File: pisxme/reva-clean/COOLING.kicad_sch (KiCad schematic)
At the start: 0 parts

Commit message: add native Phase 3 contract connectivity
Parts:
- added X: COOLING_Contract
- added XCO: COOLING_Contract, symbol PiSXMeRevAClean:COOLING_Contract
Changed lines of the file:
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@@
 (kicad_sch (version 20230409) (generator "eeschema")
   (paper "A4")
+    (symbol "PiSXMeRevAClean:COOLING_Contract"
+      (pin_names (offset 1.0))
+      (exclude_from_sim no)
+      (in_bom yes)
+      (on_board yes)
+      (property "Reference" "X"
+        (at 0 -7.039999999999999 0)
+        (effects (font (size 1.27 1.27))))
+      (property "Value" "COOLING_Contract"
+        (at 0 7.039999999999999 0)
+        (effects (font (size 1.27 1.27))))
+      (property "Footprint" ""
+        (at 0 0 0)
+        (effects (font (size 1.27 1.27)) (hide yes)))
+      (property "Datasheet" "~"
+        (at 0 0 0)
+        (effects (font (size 1.27 1.27)) (hide yes)))
+      (symbol "COOLING_Contract_1_1"
+        (rectangle (start -1.27 -5.77) (end 1.27 5.77)
+          (stroke (width 0.254) (type default)) (fill (type background)))
+        (pin passive line
+          (at -5.08 0 0)
+          (length 3.81)
+          (name "COOLING_12V" (effects (font (size 1.27 1.27))))
+          (number "1" (effects (font (size 1.27 1.27)))))
+        (pin passive line
+          (at -5.08 3 0)
+          (length 3.81)
+          (name "COOLING_PWM" (effects (font (size 1.27 1.27))))
+          (number "2" (effects (font (size 1.27 1.27)))))
+        (pin passive line
+          (at -5.08 6 0)
+          (length 3.81)
+          (name "COOLING_TACH" (effects (font (size 1.27 1.27))))
+          (number "3" (effects (font (size 1.27 1.27)))))
+        (pin passive line
+          (at -5.08 9 0)
+          (length 3.81)
+          (name "THERMAL_ALERT" (effects (font (size 1.27 1.27))))
+          (number "4" (effects (font (size 1.27 1.27)))))
+      )
+    )
   (hierarchical_label "COOLING_12V"
     (shape bidirectional)
@@
     (effects (font (size 1.27 1.27)) (justify left))
 )
-  (sheet_instances (path "/9" (page "9")))
+  (wire
+    (pts (xy 5 10) (xy 19.92 10))
+    (stroke (width 0) (type default))
 )
+  (wire
+    (pts (xy 5 13) (xy 19.92 13))
+    (stroke (width 0) (type default))
+)
+  (wire
+    (pts (xy 5 16) (xy 19.92 16))
+    (stroke (width 0) (type default))
+)
+  (wire
+    (pts (xy 5 19) (xy 19.92 19))
+    (stroke (width 0) (type default))
+)
+  (symbol
+    (lib_id "PiSXMeRevAClean:COOLING_Contract")
+    (at 25 10 0)
+    (unit 1)
+    (exclude_from_sim no)
+    (in_bom no)
+    (on_board no)
+    (dnp no)
+    (property "Reference" "XCO"
+      (at 25 5 0)
+      (effects (font (size 1.27 1.27))))
+    (property "Value" "COOLING_Contract"
+      (at 25 18 0)
+      (effects (font (size 1.27 1.27))))
+    (property "Footprint" ""
+      (at 25 10 0)
+      (effects (font (size 1.27 1.27)) (hide yes)))
+    (property "Datasheet" "~"
+      (at 25 10 0)
+      (effects (font (size 1.27 1.27)) (hide yes)))
+    (pin "1")
+    (pin "2")
+    (pin "3")
+    (pin "4")
+    (instances (project "PiSXMe_RevA_Clean"
+      (path "/30000000-0000-0000-0000-000000000000/10000000-0000-0000-0000-000000000009" (reference "XCO" ) (unit 1))))
+  )
+  (sheet_instances (path "/30000000-0000-0000-0000-000000000000/10000000-0000-0000-0000-000000000009" (page "9")))
+)

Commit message: close native Phase 3 hierarchy association
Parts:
- removed X: COOLING_Contract
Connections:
- net COOLING_12V: now also XCO.1 (COOLING_12V)
- net COOLING_PWM: now also XCO.2 (COOLING_PWM)
- net COOLING_TACH: now also XCO.3 (COOLING_TACH)
- net THERMAL_ALERT: now also XCO.4 (THERMAL_ALERT)
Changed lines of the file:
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@@
 (kicad_sch (version 20230409) (generator "eeschema")
   (paper "A4")
-    (symbol "PiSXMeRevAClean:COOLING_Contract"
-      (pin_names (offset 1.0))
-      (exclude_from_sim no)
-      (in_bom yes)
-      (on_board yes)
-      (property "Reference" "X"
-        (at 0 -7.039999999999999 0)
-        (effects (font (size 1.27 1.27))))
-      (property "Value" "COOLING_Contract"
-        (at 0 7.039999999999999 0)
-        (effects (font (size 1.27 1.27))))
-      (property "Footprint" ""
-        (at 0 0 0)
-        (effects (font (size 1.27 1.27)) (hide yes)))
-      (property "Datasheet" "~"
-        (at 0 0 0)
-        (effects (font (size 1.27 1.27)) (hide yes)))
-      (symbol "COOLING_Contract_1_1"
-        (rectangle (start -1.27 -5.77) (end 1.27 5.77)
-          (stroke (width 0.254) (type default)) (fill (type background)))
-        (pin passive line
-          (at -5.08 0 0)
-          (length 3.81)
-          (name "COOLING_12V" (effects (font (size 1.27 1.27))))
-          (number "1" (effects (font (size 1.27 1.27)))))
-        (pin passive line
-          (at -5.08 3 0)
-          (length 3.81)
-          (name "COOLING_PWM" (effects (font (size 1.27 1.27))))
-          (number "2" (effects (font (size 1.27 1.27)))))
-        (pin passive line
-          (at -5.08 6 0)
-          (length 3.81)
-          (name "COOLING_TACH" (effects (font (size 1.27 1.27))))
-          (number "3" (effects (font (size 1.27 1.27)))))
-        (pin passive line
-          (at -5.08 9 0)
-          (length 3.81)
-          (name "THERMAL_ALERT" (effects (font (size 1.27 1.27))))
-          (number "4" (effects (font (size 1.27 1.27)))))
-      )
-    )
   (hierarchical_label "COOLING_12V"
     (shape bidirectional)
-    (at 5 10 0)
-    (effects (font (size 1.27 1.27)) (justify left))
+    (at 5 10 180)
+    (effects (font (size 1.27 1.27)) (justify right))
 )
   (hierarchical_label "COOLING_PWM"
     (shape bidirectional)
-    (at 5 13 0)
-    (effects (font (size 1.27 1.27)) (justify left))
+    (at 5 13 180)
+    (effects (font (size 1.27 1.27)) (justify right))
 )
   (hierarchical_label "COOLING_TACH"
     (shape bidirectional)
-    (at 5 16 0)
-    (effects (font (size 1.27 1.27)) (justify left))
+    (at 5 16 180)
+    (effects (font (size 1.27 1.27)) (justify right))
 )
   (hierarchical_label "THERMAL_ALERT"
     (shape bidirectional)
-    (at 5 19 0)
-    (effects (font (size 1.27 1.27)) (justify left))
+    (at 5 19 180)
+    (effects (font (size 1.27 1.27)) (justify right))
 )
   (wire

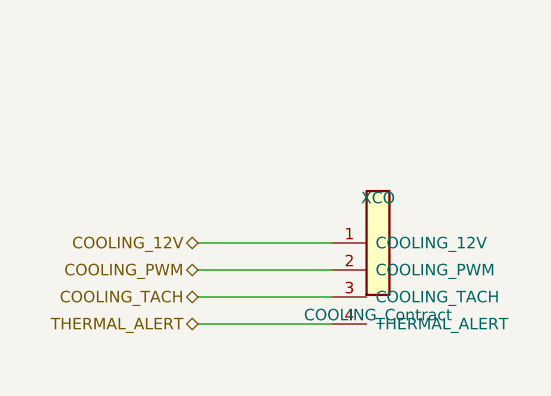
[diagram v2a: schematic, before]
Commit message: stabilize Phase 3 hierarchy netlist references
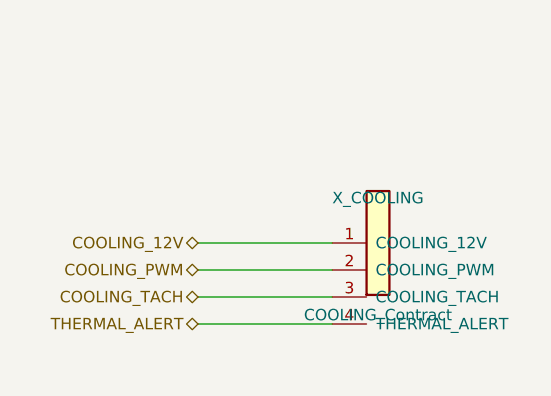
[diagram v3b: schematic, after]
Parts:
- renumbered XCO to X_COOLING
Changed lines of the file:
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@@
     (on_board no)
     (dnp no)
-    (property "Reference" "XCO"
+    (property "Reference" "X_COOLING"
       (at 25 5 0)
       (effects (font (size 1.27 1.27))))
@@
     (pin "4")
     (instances (project "PiSXMe_RevA_Clean"
-      (path "/30000000-0000-0000-0000-000000000000/10000000-0000-0000-0000-000000000009" (reference "XCO" ) (unit 1))))
+      (path "/30000000-0000-0000-0000-000000000000/10000000-0000-0000-0000-000000000009" (reference "X_COOLING" ) (unit 1))))
   )
   (sheet_instances (path "/30000000-0000-0000-0000-000000000000/10000000-0000-0000-0000-000000000009" (page "9")))

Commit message: fix KiCad annotation and netlist export
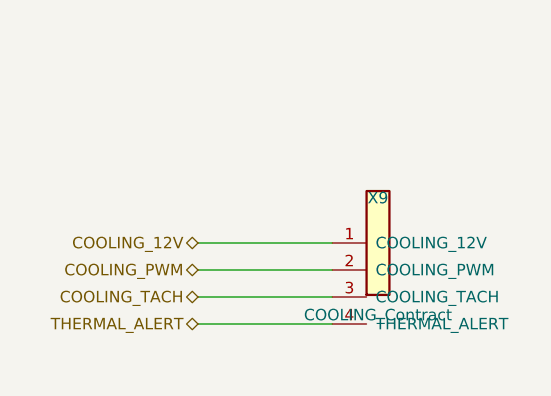
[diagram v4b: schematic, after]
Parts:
- renumbered X_COOLING to X9
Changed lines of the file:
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@@
     (on_board no)
     (dnp no)
-    (property "Reference" "X_COOLING"
+    (property "Reference" "X9"
       (at 25 5 0)
       (effects (font (size 1.27 1.27))))
@@
     (pin "4")
     (instances (project "PiSXMe_RevA_Clean"
-      (path "/30000000-0000-0000-0000-000000000000/10000000-0000-0000-0000-000000000009" (reference "X_COOLING" ) (unit 1))))
+      (path "/30000000-0000-0000-0000-000000000000/10000000-0000-0000-0000-000000000009" (reference "X9" ) (unit 1))))
   )
   (sheet_instances (path "/30000000-0000-0000-0000-000000000000/10000000-0000-0000-0000-000000000009" (page "9")))

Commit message: phase24: promote identity-preserving hierarchy repair
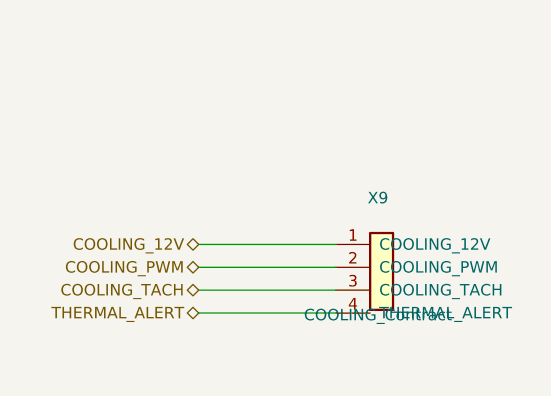
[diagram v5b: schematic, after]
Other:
- moved on the sheet: X9
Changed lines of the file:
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@@
   (hierarchical_label "COOLING_12V"
     (shape bidirectional)
-    (at 5 10 180)
+    (at 5.08 10.16 180)
     (effects (font (size 1.27 1.27)) (justify right))
 )
   (hierarchical_label "COOLING_PWM"
     (shape bidirectional)
-    (at 5 13 180)
+    (at 5.08 12.7 180)
     (effects (font (size 1.27 1.27)) (justify right))
 )
   (hierarchical_label "COOLING_TACH"
     (shape bidirectional)
-    (at 5 16 180)
+    (at 5.08 15.24 180)
     (effects (font (size 1.27 1.27)) (justify right))
 )
   (hierarchical_label "THERMAL_ALERT"
     (shape bidirectional)
-    (at 5 19 180)
+    (at 5.08 17.78 180)
     (effects (font (size 1.27 1.27)) (justify right))
 )
   (wire
-    (pts (xy 5 10) (xy 19.92 10))
+    (pts (xy 5.08 10.16) (xy 20.32 10.16))
     (stroke (width 0) (type default))
 )
   (wire
-    (pts (xy 5 13) (xy 19.92 13))
+    (pts (xy 5.08 12.7) (xy 20.32 12.7))
     (stroke (width 0) (type default))
 )
   (wire
-    (pts (xy 5 16) (xy 19.92 16))
+    (pts (xy 5.08 15.24) (xy 20.32 15.24))
     (stroke (width 0) (type default))
 )
   (wire
-    (pts (xy 5 19) (xy 19.92 19))
+    (pts (xy 5.08 17.78) (xy 20.32 17.78))
     (stroke (width 0) (type default))
 )
   (symbol
     (lib_id "PiSXMeRevAClean:COOLING_Contract")
-    (at 25 10 0)
+    (at 25.4 10.16 0)
     (unit 1)
     (exclude_from_sim no)
@@
       (effects (font (size 1.27 1.27))))
     (property "Footprint" ""
-      (at 25 10 0)
+      (at 25.4 10.16 0)
       (effects (font (size 1.27 1.27)) (hide yes)))
     (property "Datasheet" "~"
-      (at 25 10 0)
+      (at 25.4 10.16 0)
       (effects (font (size 1.27 1.27)) (hide yes)))
-    (pin "1")
+        (pin "1")
     (pin "2")
     (pin "3")
